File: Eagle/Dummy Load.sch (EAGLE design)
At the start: 59 parts, among them IC1 LM324D, IC2 AMS1117, IC3 LM35CZ, X1 MINI-USB-32005-301

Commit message: Upload Latest Version
Upload Pre-Finished Version of SCH and BOARD
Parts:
- removed D1: LED-RGB-CC-THRUCLEAR, SparkFun-LED:LED-RGB-CC-THRUCLEAR
- removed JP1: POWER_JACKSLT, SparkFun-Connectors:POWER_JACKSLT
- removed R1: 1, resistor-power:RCA4150
- removed R20: 50K, pot:TRIM_EU-CIP20C-6MM
- added D2: LED-RGB-CC, Triggerr:LED-RGB-CC
- added GOLD_ORB_SM2: OSHWLOGO_GOLD_ORB_MED, NBitWonder:OSHWLOGO_GOLD_ORB_MED
- added J2: DCJ0202, con-jack:DCJ0202
- added RW, RW2: 1, Triggerr:RESISTOR5W
- 74LS247: value TLC5916/17 -> BCD-7
- R2: value 1 -> 20k; device resistor-power:RCA4150 -> pot:3RP/1610N
- renumbered LED1 to PWR, TP1 to VREF, TP2 to PWM, TP3 to OF1, TP4 to OF2, TP5 to VG
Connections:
- new net BL: PIC.RB7/TX/CK, R23.2
- new net GL: PIC.RB6/SCK/SCL, R22.2
- net B: no longer PIC.RB7/TX/CK, R23.2
- net G: no longer PIC.RB6/SCK/SCL, R22.2
- net GND: now also D2.CC, J2.2, J2.3, R2.E, RW.1, RW2.1; no longer D1.CATHODE, JP1.GND, JP1.GNDBREAK, R1.1, R2.1, R20.E
- net N$16: now also D2.R; no longer D1.RED_CATHODE
- net N$17: now also D2.G; no longer D1.GREEN_CATHODE
- net N$18: now also D2.B; no longer D1.BLUE_CATHODE
- net OF1: no longer OF2.TP
- net OF2: now also OF2.TP
- net POT: now also R2.S; no longer R20.S
- net VCC: now also R2.A; no longer R20.A
- net VJACK: now also J2.1; no longer JP1.PWR
- net VREF: now also RW.2, RW2.2; no longer R1.2, R2.2
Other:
- note added: "Supply Stage"

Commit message: Update Proteus Files & Latest BRD Version
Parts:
- R21: value 330 -> 400
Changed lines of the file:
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@@
 <part name="GND10" library="supply1" deviceset="GND" device=""/>
 <part name="S1" library="switch-omron" deviceset="10-XX" device=""/>
-<part name="R21" library="rcl" deviceset="R-EU_" device="R0805" value="330"/>
+<part name="R21" library="rcl" deviceset="R-EU_" device="R0805" value="400"/>
 <part name="R22" library="rcl" deviceset="R-EU_" device="R0805" value="330"/>
 <part name="R23" library="rcl" deviceset="R-EU_" device="R0805" value="330"/>

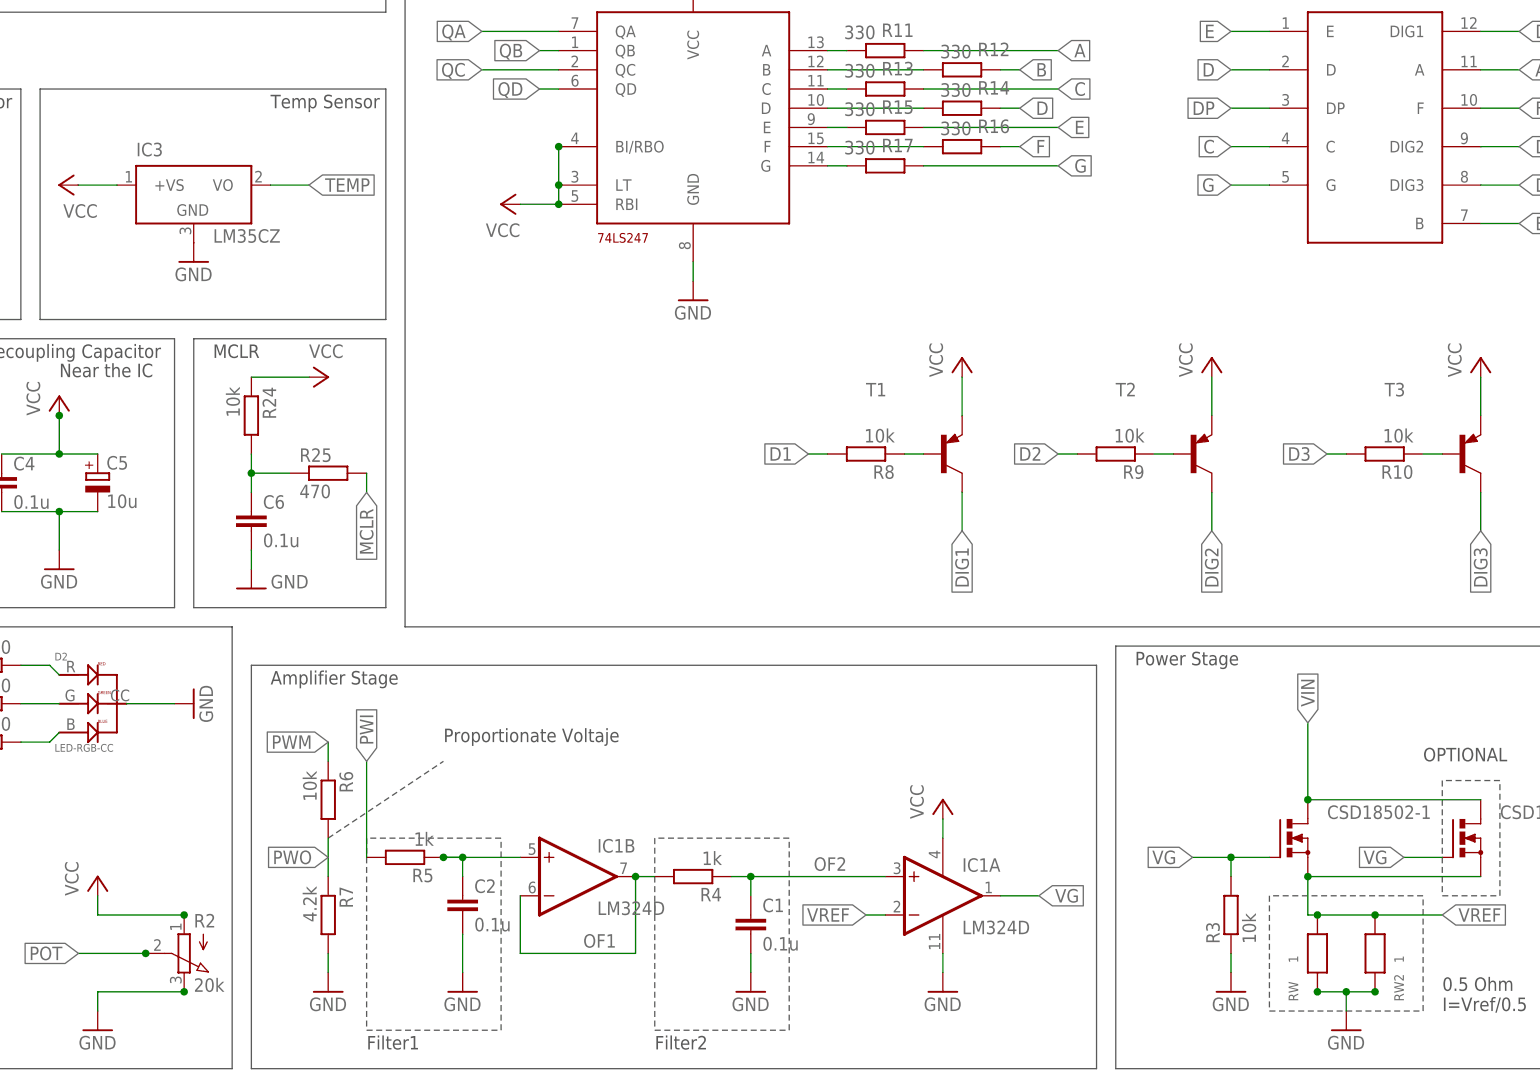
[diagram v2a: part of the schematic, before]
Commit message: Update all files to V1.1
Implement Gate Series Resistor on MOSFET, to prevent the oscillators in
the output. Also implement new OPAMP LMC662, and new desing of PCB
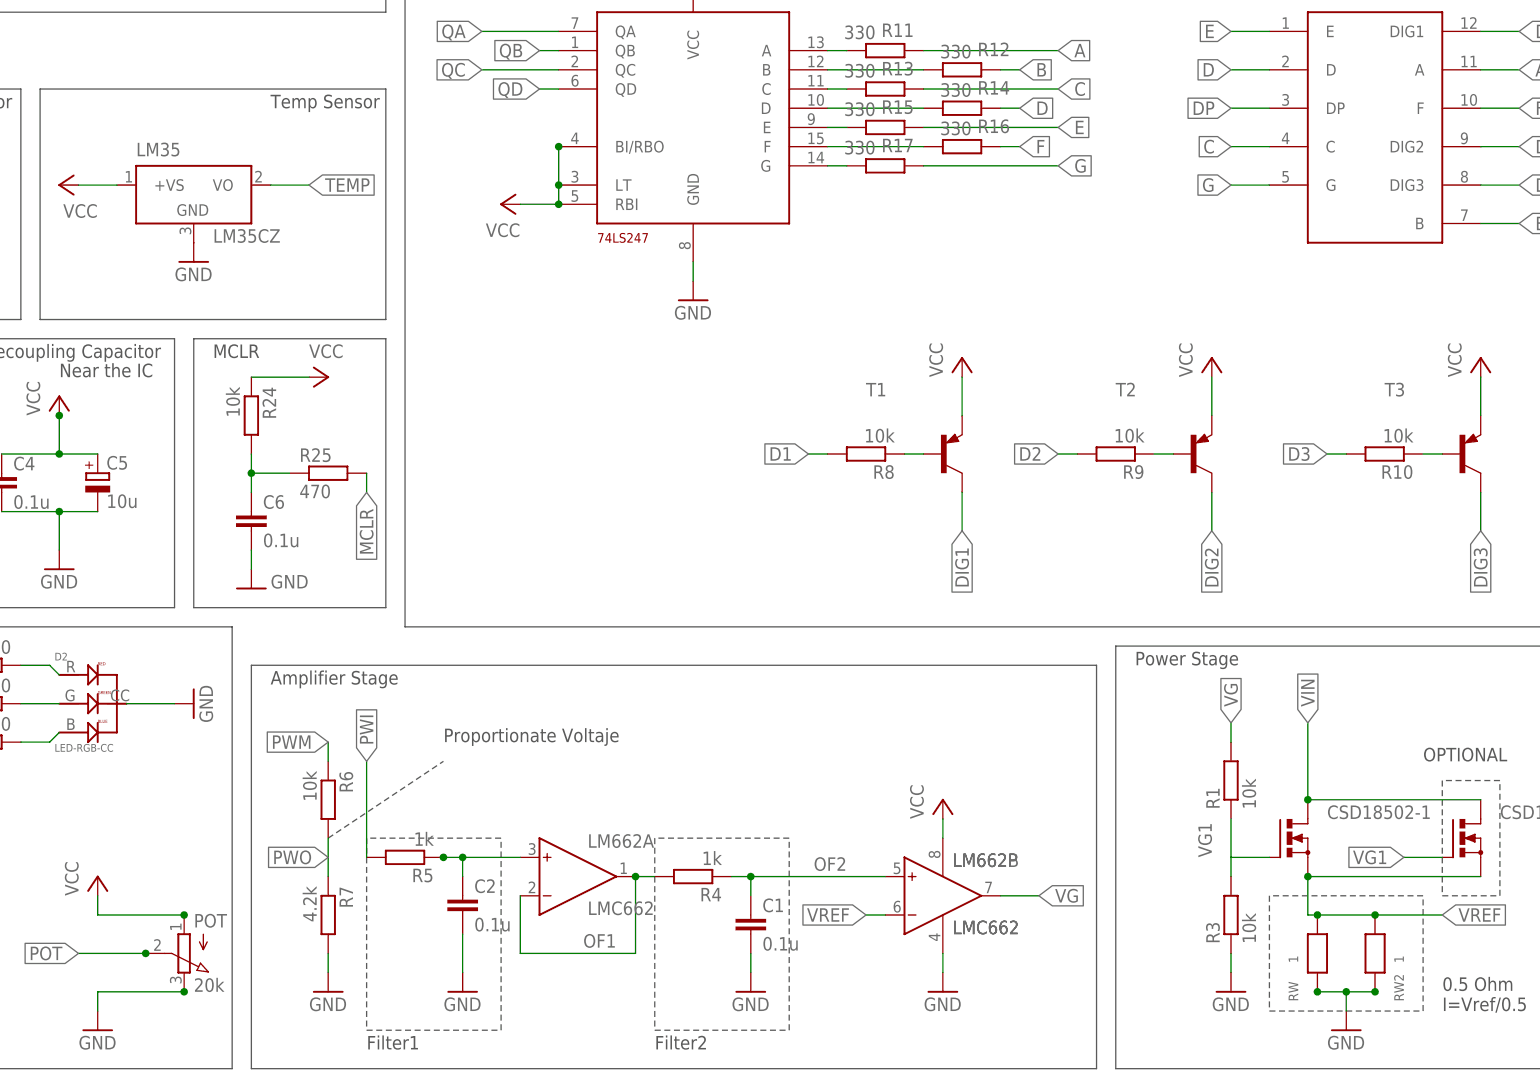
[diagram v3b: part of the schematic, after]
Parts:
- removed IC1: LM324D, linear:LM324D
- added LM662: LMC662, analog-devices:AD8033R
- added R1: 10k, rcl:R-EU_R0805
- renumbered IC3 to LM35, R2 to POT
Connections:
- new net VG1: CSD18502-1.G, CSD18502-2.G, R1.1, R3.2
- net GND: now also LM662P.V-; no longer IC1P.V-
- net N$5: now also LM662A.IN+; no longer IC1B.+IN
- net OF1: now also LM662A.IN-, LM662A.OUT; no longer IC1B.-IN, IC1B.OUT
- net OF2: now also LM662B.IN+; no longer IC1A.+IN
- net VCC: now also LM662P.V+; no longer IC1P.V+
- net VG: now also LM662B.OUT, R1.2; no longer CSD18502-1.G, CSD18502-2.G, IC1A.OUT, R3.2
- net VREF: now also LM662B.IN-; no longer IC1A.-IN
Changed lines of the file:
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@@
 <part name="R3" library="rcl" deviceset="R-EU_" device="R0805" value="10k"/>
 <part name="GND2" library="supply1" deviceset="GND" device=""/>
-<part name="IC1" library="linear" deviceset="LM324" device="D"/>
 <part name="P+1" library="supply1" deviceset="VCC" device=""/>
 <part name="GND3" library="supply1" deviceset="GND" device=""/>
@@
 <part name="C9" library="rcl" deviceset="CPOL-EU" device="153CLV-0605" value="100u"/>
 <part name="ICSP" library="pinhead" deviceset="PINHD-1X5" device=""/>
-<part name="IC3" library="lm35" deviceset="LM35" device="CZ"/>
+<part name="LM35" library="lm35" deviceset="LM35" device="CZ"/>
 <part name="P+2" library="supply1" deviceset="VCC" device=""/>
 <part name="PWR" library="led" deviceset="LED" device="CHIP-LED0805"/>
@@
 <part name="RW2" library="Triggerr" deviceset="RESISTOR5W" device="" value="1"/>
 <part name="D2" library="Triggerr" deviceset="LED-RGB-CC" device=""/>
-<part name="R2" library="pot" deviceset="3RP/1610N" device="" value="20k"/>
+<part name="POT" library="pot" deviceset="3RP/1610N" device="" value="20k"/>
 <part name="GND22" library="supply1" deviceset="GND" device=""/>
 <part name="GND23" library="supply1" deviceset="GND" device=""/>
@@
 <part name="GOLD_ORB_SM2" library="NBitWonder" deviceset="OSHWLOGO" device="_GOLD_ORB_MED"/>
 <part name="J2" library="con-jack" deviceset="DCJ0202" device=""/>
+<part name="LM662" library="analog-devices" deviceset="AD8033" device="R" value="LMC662"/>
+<part name="R1" library="rcl" deviceset="R-EU_" device="R0805" value="10k"/>
 </parts>
 <sheets>
@@
 <instance part="R3" gate="G$1" x="213.36" y="5.08" rot="R90"/>
 <instance part="GND2" gate="1" x="213.36" y="-5.08"/>
-<instance part="IC1" gate="A" x="175.26" y="7.62"/>
-<instance part="IC1" gate="B" x="127" y="10.16"/>
-<instance part="IC1" gate="P" x="175.26" y="7.62"/>
 <instance part="P+1" gate="VCC" x="175.26" y="20.32"/>
 <instance part="GND3" gate="1" x="175.26" y="-5.08"/>
@@
 <instance part="C9" gate="G$1" x="-30.48" y="43.18"/>
 <instance part="ICSP" gate="A" x="-17.78" y="101.6" rot="R90"/>
-<instance part="IC3" gate="G$1" x="76.2" y="101.6"/>
+<instance part="LM35" gate="G$1" x="76.2" y="101.6"/>
 <instance part="P+2" gate="VCC" x="58.42" y="101.6" smashed="yes" rot="R90">
 <attribute name="VALUE" x="63.5" y="99.06" size="1.778" layer="96" rot="R180"/>
@@
 </instance>
 <instance part="D2" gate="G$1" x="62.23" y="35.56"/>
-<instance part="R2" gate="G$1" x="74.93" y="0" smashed="yes" rot="R180">
+<instance part="POT" gate="G$1" x="74.93" y="0" smashed="yes" rot="R180">
 <attribute name="NAME" x="76.2" y="3.429" size="1.778" layer="95"/>
 <attribute name="VALUE" x="76.2" y="-5.08" size="1.778" layer="96"/>
@@
 <instance part="GOLD_ORB_SM2" gate="G$1" x="-83.82" y="124.46"/>
 <instance part="J2" gate="G$1" x="-66.04" y="17.78"/>
+<instance part="LM662" gate="A" x="124.46" y="10.16"/>
+<instance part="LM662" gate="B" x="172.72" y="7.62"/>
+<instance part="LM662" gate="P" x="175.26" y="7.62"/>
+<instance part="R1" gate="G$1" x="213.36" y="22.86" rot="R90"/>
 </instances>
 <busses>
@@
 </segment>
 <segment>
-<pinref part="IC1" gate="A" pin="-IN"/>
 <wire x1="167.64" y1="5.08" x2="165.1" y2="5.08" width="0.1524" layer="91"/>
 <label x="165.1" y="5.08" size="1.778" layer="95" rot="R180" xref="yes"/>
+<pinref part="LM662" gate="B" pin="IN-"/>
 </segment>
 <segment>
@@
 <segment>
 <pinref part="GND3" gate="1" pin="GND"/>
-<pinref part="IC1" gate="P" pin="V-"/>
 <wire x1="175.26" y1="-2.54" x2="175.26" y2="0" width="0.1524" layer="91"/>
+<pinref part="LM662" gate="P" pin="V-"/>
 </segment>
 <segment>
@@
 <wire x1="74.93" y1="-5.08" x2="63.5" y2="-5.08" width="0.1524" layer="91"/>
 <wire x1="63.5" y1="-5.08" x2="63.5" y2="-7.62" width="0.1524" layer="91"/>
-<pinref part="R2" gate="G$1" pin="E"/>
+<pinref part="POT" gate="G$1" pin="E"/>
 <junction x="74.93" y="-5.08"/>
 </segment>
@@
 </segment>
 <segment>
-<pinref part="IC3" gate="G$1" pin="GND"/>
+<pinref part="LM35" gate="G$1" pin="GND"/>
 <pinref part="GND17" gate="1" pin="GND"/>
 </segment>
@@
 <net name="VG" class="0">
 <segment>
-<pinref part="CSD18502-1" gate="G$1" pin="G"/>
-<wire x1="218.44" y1="12.7" x2="213.36" y2="12.7" width="0.1524" layer="91"/>
-<label x="208.28" y="12.7" size="1.778" layer="95" rot="R180" xref="yes"/>
-<pinref part="R3" gate="G$1" pin="2"/>
-<wire x1="213.36" y1="12.7" x2="208.28" y2="12.7" width="0.1524" layer="91"/>
-<wire x1="213.36" y1="10.16" x2="213.36" y2="12.7" width="0.1524" layer="91"/>
-<junction x="213.36" y="12.7"/>
-</segment>
-<segment>
-<pinref part="CSD18502-2" gate="G$1" pin="G"/>
-<wire x1="241.3" y1="12.7" x2="236.22" y2="12.7" width="0.1524" layer="91"/>
-<label x="236.22" y="12.7" size="1.778" layer="95" rot="R180" xref="yes"/>
-</segment>
-<segment>
-<pinref part="IC1" gate="A" pin="OUT"/>
 <wire x1="182.88" y1="7.62" x2="187.96" y2="7.62" width="0.1524" layer="91"/>
 <label x="187.96" y="7.62" size="1.778" layer="95" xref="yes"/>
+<pinref part="LM662" gate="B" pin="OUT"/>
 </segment>
 <segment>
@@
 <label x="-45.72" y="81.28" size="1.778" layer="95" rot="R90" xref="yes"/>
 </segment>
+<segment>
+<pinref part="R1" gate="G$1" pin="2"/>
+<wire x1="213.36" y1="27.94" x2="213.36" y2="30.48" width="0.1524" layer="91"/>
+<label x="213.36" y="30.48" size="1.778" layer="95" rot="R90" xref="yes"/>
+</segment>
 </net>
 <net name="VCC" class="0">
 <segment>
-<pinref part="IC1" gate="P" pin="V+"/>
 <pinref part="P+1" gate="VCC" pin="VCC"/>
 <wire x1="175.26" y1="15.24" x2="175.26" y2="17.78" width="0.1524" layer="91"/>
+<pinref part="LM662" gate="P" pin="V+"/>
 </segment>
 <segment>
@@
 <wire x1="74.93" y1="5.08" x2="63.5" y2="5.08" width="0.1524" layer="91"/>
 <wire x1="63.5" y1="5.08" x2="63.5" y2="7.62" width="0.1524" layer="91"/>
-<pinref part="R2" gate="G$1" pin="A"/>
+<pinref part="POT" gate="G$1" pin="A"/>
 <junction x="74.93" y="5.08"/>
 </segment>
@@
 </segment>
 <segment>
-<pinref part="IC3" gate="G$1" pin="+VS"/>
+<pinref part="LM35" gate="G$1" pin="+VS"/>
 <pinref part="P+2" gate="VCC" pin="VCC"/>
 <wire x1="66.04" y1="101.6" x2="60.96" y2="101.6" width="0.1524" layer="91"/>
@@
 <net name="OF2" class="0">
 <segment>
-<pinref part="IC1" gate="A" pin="+IN"/>
 <pinref part="R4" gate="G$1" pin="1"/>
 <wire x1="167.64" y1="10.16" x2="149.86" y2="10.16" width="0.1524" layer="91"/>
@@
 <label x="162.56" y="12.7" size="1.778" layer="95" rot="R180"/>
 <junction x="149.86" y="10.16"/>
+<pinref part="LM662" gate="B" pin="IN+"/>
 </segment>
 <segment>
@@
 <net name="OF1" class="0">
 <segment>
-<pinref part="IC1" gate="B" pin="OUT"/>
 <pinref part="R4" gate="G$1" pin="2"/>
 <wire x1="134.62" y1="10.16" x2="137.16" y2="10.16" width="0.1524" layer="91"/>
-<pinref part="IC1" gate="B" pin="-IN"/>
 <wire x1="119.38" y1="7.62" x2="119.38" y2="0" width="0.1524" layer="91"/>
 <wire x1="119.38" y1="0" x2="134.62" y2="0" width="0.1524" layer="91"/>
 <wire x1="134.62" y1="0" x2="134.62" y2="10.16" width="0.1524" layer="91"/>
 <label x="132.08" y="2.54" size="1.778" layer="95" rot="R180"/>
+<pinref part="LM662" gate="A" pin="IN-"/>
+<pinref part="LM662" gate="A" pin="OUT"/>
 <junction x="134.62" y="10.16"/>
 </segment>
@@
 <net name="N$5" class="0">
 <segment>
-<pinref part="IC1" gate="B" pin="+IN"/>
 <pinref part="R5" gate="G$1" pin="1"/>
 <wire x1="119.38" y1="12.7" x2="111.76" y2="12.7" width="0.1524" layer="91"/>
 <pinref part="C2" gate="G$1" pin="1"/>
-<wire x1="111.76" y1="12.7" x2="109.22" y2="12.7" width="0.1524" layer="91"/>
 <wire x1="109.22" y1="12.7" x2="111.76" y2="12.7" width="0.1524" layer="91"/>
 <wire x1="111.76" y1="12.7" x2="111.76" y2="10.16" width="0.1524" layer="91"/>
 <junction x="111.76" y="12.7"/>
 <junction x="109.22" y="12.7"/>
+<pinref part="LM662" gate="A" pin="IN+"/>
 </segment>
 </net>
@@
 <label x="60.96" y="0" size="1.778" layer="95" rot="R180" xref="yes"/>
 <wire x1="60.96" y1="0" x2="69.85" y2="0" width="0.1524" layer="91"/>
-<pinref part="R2" gate="G$1" pin="S"/>
+<pinref part="POT" gate="G$1" pin="S"/>
 <junction x="69.85" y="0"/>
 </segment>
@@
 <net name="TEMP" class="0">
 <segment>
-<pinref part="IC3" gate="G$1" pin="VO"/>
+<pinref part="LM35" gate="G$1" pin="VO"/>
 <wire x1="86.36" y1="101.6" x2="91.44" y2="101.6" width="0.1524" layer="91"/>
 <label x="91.44" y="101.6" size="1.778" layer="95" xref="yes"/>
@@
 </segment>
 </net>
+<net name="VG1" class="0">
+<segment>
+<pinref part="CSD18502-2" gate="G$1" pin="G"/>
+<wire x1="241.3" y1="12.7" x2="236.22" y2="12.7" width="0.1524" layer="91"/>
+<label x="236.22" y="12.7" size="1.778" layer="95" rot="R180" xref="yes"/>
+</segment>
+<segment>
+<pinref part="CSD18502-1" gate="G$1" pin="G"/>
+<pinref part="R3" gate="G$1" pin="2"/>
+<wire x1="213.36" y1="12.7" x2="218.44" y2="12.7" width="0.1524" layer="91"/>
+<wire x1="213.36" y1="10.16" x2="213.36" y2="12.7" width="0.1524" layer="91"/>
+<wire x1="213.36" y1="12.7" x2="213.36" y2="17.78" width="0.1524" layer="91"/>
+<pinref part="R1" gate="G$1" pin="1"/>
+<label x="210.82" y="12.7" size="1.778" layer="95" rot="R90"/>
+</segment>
+</net>
